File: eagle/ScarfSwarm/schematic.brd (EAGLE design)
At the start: 21.6 x 50.8 mm, 5 parts

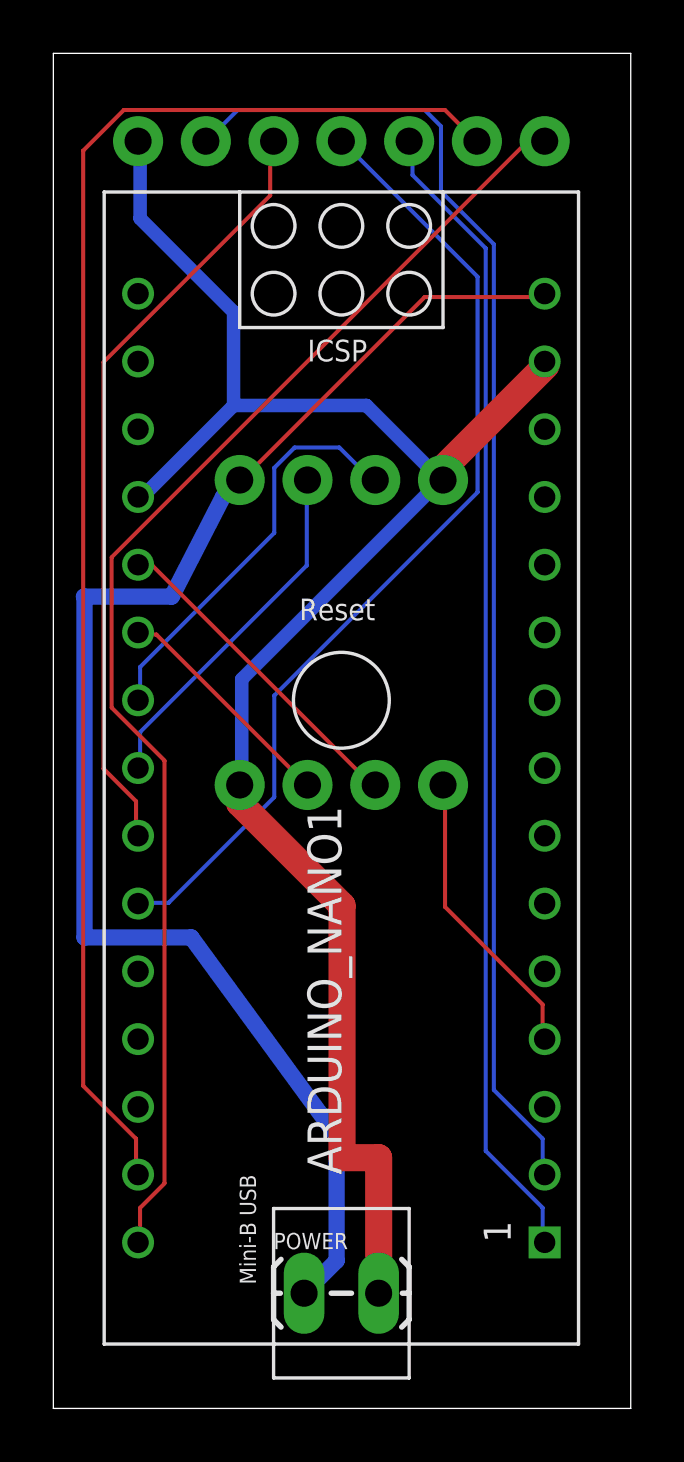
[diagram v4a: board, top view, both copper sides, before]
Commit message: v1.1 Fatten some of the leads
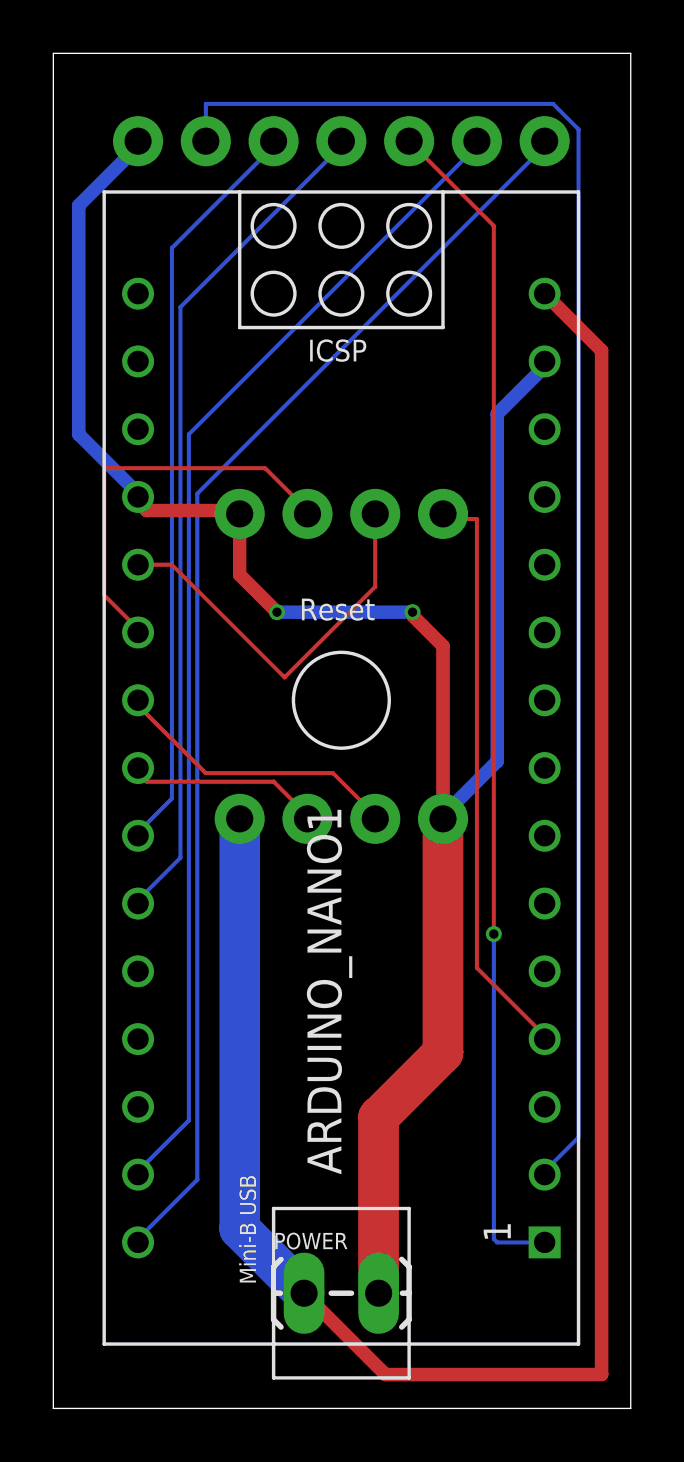
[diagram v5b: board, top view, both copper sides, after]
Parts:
- moved LEDSTRIP 12.7 mm to (13.3, 20.8)
- moved ROTARY 10.2 mm to (13.3, 32.3)
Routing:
- net N$12: track 55.2 -> 72.6 mm
- net N$5: track 55.1 -> 44.0 mm
- net N$11: track 11.1 -> 22.0 mm
- net GND: track 68.1 -> 74.5 mm, vias 0 -> 2
- net N$9: track 8.72 -> 15.1 mm
- net N$13: track 13.4 -> 7.33 mm
- net N$1: track 50.4 -> 55.5 mm
- net N$3: track 36.6 -> 31.7 mm
- net N$8: track 15.5 -> 10.9 mm
- net N$10: track 12.3 -> 14.8 mm
- net N$6: track 49.6 -> 47.6 mm
- net N$2: track 29.2 -> 28.1 mm
- net N$4: track 43.4 -> 44.4 mm, vias 0 -> 1
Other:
- board text added: "v1.1 Jul 30, 2019"
- board text removed: "v1.0 Jul 29, 2019"

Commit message: scarfymcscarfface
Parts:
- renumbered ARDUINO_NANO1 to SCARFYMCSCARFFACE
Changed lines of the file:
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@@
 <layers>
 <layer number="1" name="Top" color="4" fill="1" visible="yes" active="yes"/>
-<layer number="16" name="Bottom" color="1" fill="1" visible="yes" active="yes"/>
+<layer number="16" name="Bottom" color="1" fill="1" visible="no" active="yes"/>
 <layer number="17" name="Pads" color="2" fill="1" visible="yes" active="yes"/>
 <layer number="18" name="Vias" color="2" fill="1" visible="yes" active="yes"/>
 <layer number="19" name="Unrouted" color="6" fill="1" visible="yes" active="yes"/>
 <layer number="20" name="Dimension" color="24" fill="1" visible="yes" active="yes"/>
-<layer number="21" name="tPlace" color="7" fill="1" visible="no" active="yes"/>
-<layer number="22" name="bPlace" color="7" fill="1" visible="yes" active="yes"/>
-<layer number="23" name="tOrigins" color="15" fill="1" visible="no" active="yes"/>
-<layer number="24" name="bOrigins" color="15" fill="1" visible="yes" active="yes"/>
-<layer number="25" name="tNames" color="7" fill="1" visible="no" active="yes"/>
-<layer number="26" name="bNames" color="7" fill="1" visible="yes" active="yes"/>
+<layer number="21" name="tPlace" color="7" fill="1" visible="yes" active="yes"/>
+<layer number="22" name="bPlace" color="7" fill="1" visible="no" active="yes"/>
+<layer number="23" name="tOrigins" color="15" fill="1" visible="yes" active="yes"/>
+<layer number="24" name="bOrigins" color="15" fill="1" visible="no" active="yes"/>
+<layer number="25" name="tNames" color="7" fill="1" visible="yes" active="yes"/>
+<layer number="26" name="bNames" color="7" fill="1" visible="no" active="yes"/>
 <layer number="27" name="tValues" color="7" fill="1" visible="no" active="yes"/>
 <layer number="28" name="bValues" color="7" fill="1" visible="no" active="yes"/>
@@
 <layer number="37" name="tTest" color="7" fill="1" visible="no" active="yes"/>
 <layer number="38" name="bTest" color="7" fill="1" visible="no" active="yes"/>
-<layer number="39" name="tKeepout" color="4" fill="11" visible="no" active="yes"/>
-<layer number="40" name="bKeepout" color="1" fill="11" visible="yes" active="yes"/>
-<layer number="41" name="tRestrict" color="4" fill="10" visible="no" active="yes"/>
-<layer number="42" name="bRestrict" color="1" fill="10" visible="yes" active="yes"/>
+<layer number="39" name="tKeepout" color="4" fill="11" visible="yes" active="yes"/>
+<layer number="40" name="bKeepout" color="1" fill="11" visible="no" active="yes"/>
+<layer number="41" name="tRestrict" color="4" fill="10" visible="yes" active="yes"/>
+<layer number="42" name="bRestrict" color="1" fill="10" visible="no" active="yes"/>
 <layer number="43" name="vRestrict" color="2" fill="10" visible="no" active="yes"/>
 <layer number="44" name="Drills" color="7" fill="1" visible="no" active="yes"/>
@@
 <layer number="49" name="Reference" color="7" fill="1" visible="no" active="yes"/>
 <layer number="50" name="dxf" color="7" fill="1" visible="no" active="no"/>
-<layer number="51" name="tDocu" color="7" fill="1" visible="no" active="yes"/>
-<layer number="52" name="bDocu" color="7" fill="1" visible="yes" active="yes"/>
+<layer number="51" name="tDocu" color="7" fill="1" visible="yes" active="yes"/>
+<layer number="52" name="bDocu" color="7" fill="1" visible="no" active="yes"/>
 <layer number="53" name="tGND_GNDA" color="7" fill="9" visible="no" active="no"/>
 <layer number="54" name="bGND_GNDA" color="1" fill="9" visible="no" active="no"/>
@@
 <attribute name="VALUE" x="6.985" y="0.762" size="0.6096" layer="27" font="vector" ratio="20"/>
 </element>
-<element name="ARDUINO_NANO1" library="ArduinoNanoV30" package="ARDUINO_NANO" value="" x="9.525" y="25.273" smashed="yes" rot="R90">
+<element name="SCARFYMCSCARFFACE" library="ArduinoNanoV30" package="ARDUINO_NANO" value="" x="9.525" y="25.273" smashed="yes" rot="R90">
 <attribute name="NAME" x="9.525" y="7.493" size="1.27" layer="21" font="vector" rot="R90"/>
 <attribute name="VALUE" x="12.065" y="7.493" size="1.27" layer="21" font="vector" rot="R90"/>
@@
 <contactref element="ROTARY" pad="4"/>
 <contactref element="POWER" pad="2"/>
-<contactref element="ARDUINO_NANO1" pad="19"/>
-<contactref element="ARDUINO_NANO1" pad="14"/>
+<contactref element="SCARFYMCSCARFFACE" pad="19"/>
+<contactref element="SCARFYMCSCARFFACE" pad="14"/>
 <wire x1="10.922" y1="3.048" x2="10.922" y2="9.652" width="1.524" layer="1"/>
 <wire x1="13.335" y1="12.065" x2="13.335" y2="20.828" width="1.524" layer="1"/>
@@
 <signal name="N$1">
 <contactref element="RFCONN" pad="6"/>
-<contactref element="ARDUINO_NANO1" pad="2"/>
+<contactref element="SCARFYMCSCARFFACE" pad="2"/>
 <wire x1="18.415" y1="8.89" x2="17.145" y2="7.62" width="0.1524" layer="16"/>
 <wire x1="18.415" y1="46.6725" x2="18.415" y2="8.89" width="0.1524" layer="16"/>
@@
 <signal name="N$2">
 <contactref element="RFCONN" pad="5"/>
-<contactref element="ARDUINO_NANO1" pad="24"/>
+<contactref element="SCARFYMCSCARFFACE" pad="24"/>
 <wire x1="3.175" y1="21.59" x2="1.905" y2="20.32" width="0.1524" layer="16"/>
 <wire x1="3.175" y1="42.2275" x2="3.175" y2="21.59" width="0.1524" layer="16"/>
@@
 <signal name="N$3">
 <contactref element="RFCONN" pad="4"/>
-<contactref element="ARDUINO_NANO1" pad="25"/>
+<contactref element="SCARFYMCSCARFFACE" pad="25"/>
 <wire x1="3.4925" y1="19.3675" x2="1.905" y2="17.78" width="0.1524" layer="16"/>
 <wire x1="3.4925" y1="40.005" x2="3.4925" y2="19.3675" width="0.1524" layer="16"/>
@@
 <signal name="N$4">
 <contactref element="RFCONN" pad="3"/>
-<contactref element="ARDUINO_NANO1" pad="1"/>
+<contactref element="SCARFYMCSCARFFACE" pad="1"/>
 <wire x1="12.065" y1="46.228" x2="15.24" y2="43.053" width="0.1524" layer="1"/>
 <via x="15.24" y="16.51" extent="1-16" drill="0.35"/>
@@
 <signal name="N$5">
 <contactref element="RFCONN" pad="2"/>
-<contactref element="ARDUINO_NANO1" pad="29"/>
+<contactref element="SCARFYMCSCARFFACE" pad="29"/>
 <wire x1="3.81" y1="9.525" x2="1.905" y2="7.62" width="0.1524" layer="16"/>
 <wire x1="3.81" y1="35.2425" x2="3.81" y2="9.525" width="0.1524" layer="16"/>
@@
 <signal name="N$6">
 <contactref element="RFCONN" pad="1"/>
-<contactref element="ARDUINO_NANO1" pad="30"/>
+<contactref element="SCARFYMCSCARFFACE" pad="30"/>
 <wire x1="4.1275" y1="7.3025" x2="1.905" y2="5.08" width="0.1524" layer="16"/>
 <wire x1="4.1275" y1="33.02" x2="4.1275" y2="7.3025" width="0.1524" layer="16"/>
@@
 <signal name="N$8">
 <contactref element="LEDSTRIP" pad="2"/>
-<contactref element="ARDUINO_NANO1" pad="22"/>
+<contactref element="SCARFYMCSCARFFACE" pad="22"/>
 <wire x1="4.445" y1="22.5425" x2="1.905" y2="25.0825" width="0.1524" layer="1"/>
 <wire x1="9.2075" y1="22.5425" x2="4.445" y2="22.5425" width="0.1524" layer="1"/>
@@
 <signal name="N$9">
 <contactref element="ROTARY" pad="3"/>
-<contactref element="ARDUINO_NANO1" pad="21"/>
+<contactref element="SCARFYMCSCARFFACE" pad="21"/>
 <wire x1="0.635" y1="29.21" x2="1.905" y2="27.94" width="0.1524" layer="1"/>
 <wire x1="0.635" y1="33.9725" x2="0.635" y2="29.21" width="0.1524" layer="1"/>
@@
 <signal name="N$10">
 <contactref element="ROTARY" pad="2"/>
-<contactref element="ARDUINO_NANO1" pad="20"/>
+<contactref element="SCARFYMCSCARFFACE" pad="20"/>
 <wire x1="1.905" y1="30.353" x2="3.175" y2="30.353" width="0.1524" layer="1"/>
 <wire x1="7.39775" y1="26.13025" x2="3.175" y2="30.353" width="0.1524" layer="1"/>
@@
 <signal name="N$11">
 <contactref element="ROTARY" pad="1"/>
-<contactref element="ARDUINO_NANO1" pad="4"/>
+<contactref element="SCARFYMCSCARFFACE" pad="4"/>
 <wire x1="14.605" y1="15.24" x2="17.145" y2="12.7" width="0.1524" layer="1"/>
 <wire x1="14.605" y1="32.0675" x2="14.605" y2="15.24" width="0.1524" layer="1"/>
@@
 <contactref element="LEDSTRIP" pad="4"/>
 <contactref element="POWER" pad="1"/>
-<contactref element="ARDUINO_NANO1" pad="15"/>
+<contactref element="SCARFYMCSCARFFACE" pad="15"/>
 <wire x1="8.128" y1="3.048" x2="5.715" y2="5.461" width="1.524" layer="16"/>
 <wire x1="5.715" y1="5.461" x2="5.715" y2="20.828" width="1.524" layer="16"/>
@@
 <signal name="N$13">
 <contactref element="LEDSTRIP" pad="3"/>
-<contactref element="ARDUINO_NANO1" pad="23"/>
+<contactref element="SCARFYMCSCARFFACE" pad="23"/>
 <wire x1="2.2225" y1="22.225" x2="1.905" y2="22.5425" width="0.1524" layer="1"/>
 <wire x1="6.985" y1="22.225" x2="2.2225" y2="22.225" width="0.1524" layer="1"/>
@@
 </signal>
 <signal name="5V">
-<contactref element="ARDUINO_NANO1" pad="12"/>
+<contactref element="SCARFYMCSCARFFACE" pad="12"/>
 </signal>
 </signals>

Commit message: silk screen change
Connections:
- new net N$7: SCARFYMCSCARFFACE.26
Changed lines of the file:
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@@
 <grid distance="50" unitdist="mil" unit="mil" style="lines" multiple="1" display="yes" altdistance="5" altunitdist="mil" altunit="mil"/>
 <layers>
-<layer number="1" name="Top" color="4" fill="1" visible="yes" active="yes"/>
-<layer number="16" name="Bottom" color="1" fill="1" visible="no" active="yes"/>
+<layer number="1" name="Top" color="4" fill="1" visible="no" active="yes"/>
+<layer number="16" name="Bottom" color="1" fill="1" visible="yes" active="yes"/>
 <layer number="17" name="Pads" color="2" fill="1" visible="yes" active="yes"/>
 <layer number="18" name="Vias" color="2" fill="1" visible="yes" active="yes"/>
 <layer number="19" name="Unrouted" color="6" fill="1" visible="yes" active="yes"/>
 <layer number="20" name="Dimension" color="24" fill="1" visible="yes" active="yes"/>
-<layer number="21" name="tPlace" color="7" fill="1" visible="yes" active="yes"/>
-<layer number="22" name="bPlace" color="7" fill="1" visible="no" active="yes"/>
-<layer number="23" name="tOrigins" color="15" fill="1" visible="yes" active="yes"/>
-<layer number="24" name="bOrigins" color="15" fill="1" visible="no" active="yes"/>
-<layer number="25" name="tNames" color="7" fill="1" visible="yes" active="yes"/>
-<layer number="26" name="bNames" color="7" fill="1" visible="no" active="yes"/>
+<layer number="21" name="tPlace" color="7" fill="1" visible="no" active="yes"/>
+<layer number="22" name="bPlace" color="7" fill="1" visible="yes" active="yes"/>
+<layer number="23" name="tOrigins" color="15" fill="1" visible="no" active="yes"/>
+<layer number="24" name="bOrigins" color="15" fill="1" visible="yes" active="yes"/>
+<layer number="25" name="tNames" color="7" fill="1" visible="no" active="yes"/>
+<layer number="26" name="bNames" color="7" fill="1" visible="yes" active="yes"/>
 <layer number="27" name="tValues" color="7" fill="1" visible="no" active="yes"/>
 <layer number="28" name="bValues" color="7" fill="1" visible="no" active="yes"/>
@@
 <layer number="37" name="tTest" color="7" fill="1" visible="no" active="yes"/>
 <layer number="38" name="bTest" color="7" fill="1" visible="no" active="yes"/>
-<layer number="39" name="tKeepout" color="4" fill="11" visible="yes" active="yes"/>
-<layer number="40" name="bKeepout" color="1" fill="11" visible="no" active="yes"/>
-<layer number="41" name="tRestrict" color="4" fill="10" visible="yes" active="yes"/>
-<layer number="42" name="bRestrict" color="1" fill="10" visible="no" active="yes"/>
+<layer number="39" name="tKeepout" color="4" fill="11" visible="no" active="yes"/>
+<layer number="40" name="bKeepout" color="1" fill="11" visible="yes" active="yes"/>
+<layer number="41" name="tRestrict" color="4" fill="10" visible="no" active="yes"/>
+<layer number="42" name="bRestrict" color="1" fill="10" visible="yes" active="yes"/>
 <layer number="43" name="vRestrict" color="2" fill="10" visible="no" active="yes"/>
 <layer number="44" name="Drills" color="7" fill="1" visible="no" active="yes"/>
@@
 <layer number="49" name="Reference" color="7" fill="1" visible="no" active="yes"/>
 <layer number="50" name="dxf" color="7" fill="1" visible="no" active="no"/>
-<layer number="51" name="tDocu" color="7" fill="1" visible="yes" active="yes"/>
-<layer number="52" name="bDocu" color="7" fill="1" visible="no" active="yes"/>
+<layer number="51" name="tDocu" color="7" fill="1" visible="no" active="yes"/>
+<layer number="52" name="bDocu" color="7" fill="1" visible="yes" active="yes"/>
 <layer number="53" name="tGND_GNDA" color="7" fill="9" visible="no" active="no"/>
 <layer number="54" name="bGND_GNDA" color="1" fill="9" visible="no" active="no"/>
@@
 <contactref element="SCARFYMCSCARFFACE" pad="12"/>
 </signal>
+<signal name="N$7">
+<contactref element="SCARFYMCSCARFFACE" pad="26"/>
+</signal>
 </signals>

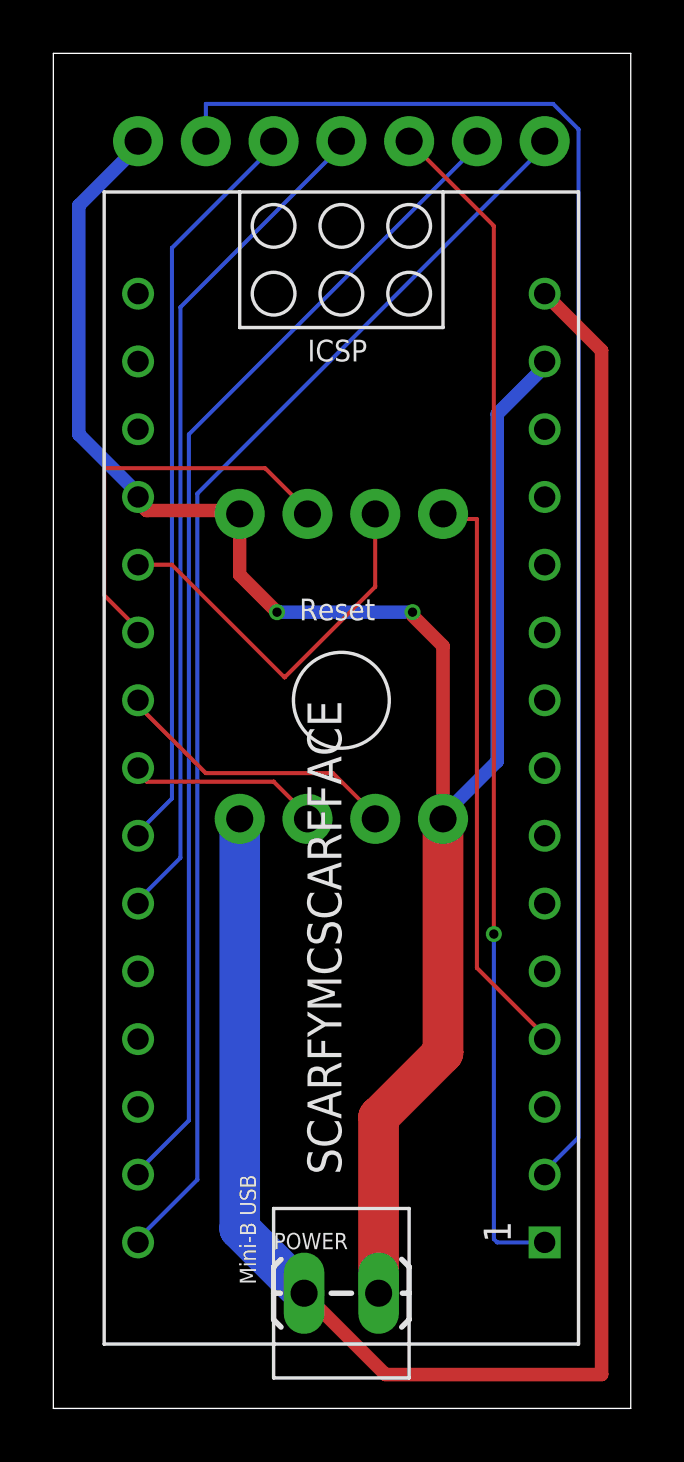
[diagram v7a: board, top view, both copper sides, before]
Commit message: reorder radio contacts so that they are easy to solder
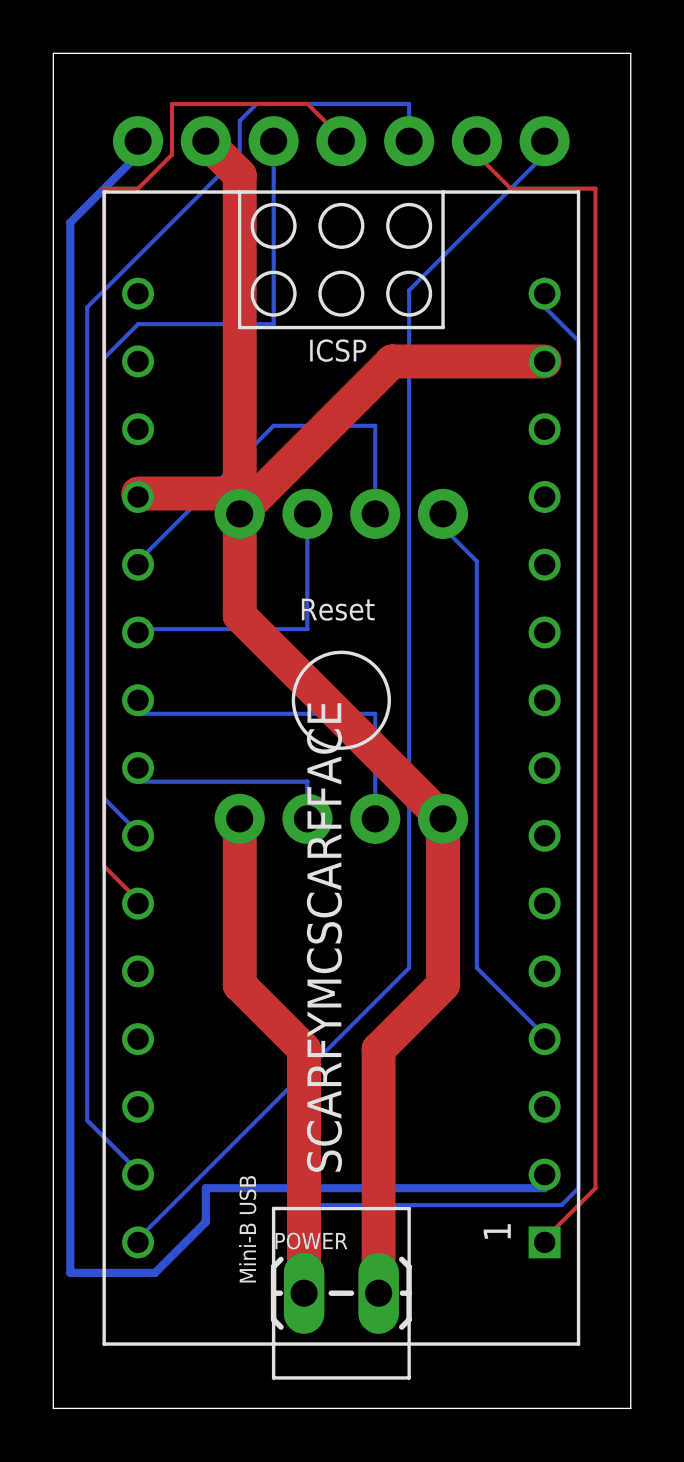
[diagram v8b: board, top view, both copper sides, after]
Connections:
- removed net N$7 (its old number): SCARFYMCSCARFFACE.26
- net GND: now also RFCONN.6; no longer RFCONN.7
- net N$1: now also RFCONN.7; no longer RFCONN.6
- net N$4: now also RFCONN.2; no longer RFCONN.3
- net N$5: now also RFCONN.3; no longer RFCONN.2
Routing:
- net GND: track 74.5 -> 65.6 mm, vias 2 -> 0
- net N$1: track 55.5 -> 63.8 mm
- net N$3: track 31.7 -> 39.3 mm
- net N$5: track 44.0 -> 50.7 mm
- net N$12: track 72.6 -> 66.6 mm
- net N$9: track 15.1 -> 10.8 mm
- net N$2: track 28.1 -> 32.2 mm
- net N$8: track 10.9 -> 13.3 mm
- net N$4: track 44.4 -> 45.8 mm, vias 1 -> 0
- net N$13: track 7.33 -> 8.26 mm
- net N$11: track 22.0 -> 21.3 mm
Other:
- board text added: "11/MO"
- board text added: "12/MI"
- board text added: "13/SCK"
- board text added: "6/CE"
- board text added: "7/CSN"
- board text added: "v1.2.0 Aug 2, 2019"
- board text removed: "13"
- board text removed: "D12"
- board text removed: "D6"
- board text removed: "D7"
- board text removed: "MOSI/D11"
- board text removed: "v1.1 Jul 30, 2019"
